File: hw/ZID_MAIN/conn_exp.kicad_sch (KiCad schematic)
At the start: 64 parts, among them J10 USB-C PWR ONLY, J8 BRK EXP SOCKET, J9 Z80-TARGET, U24 74AHCT125

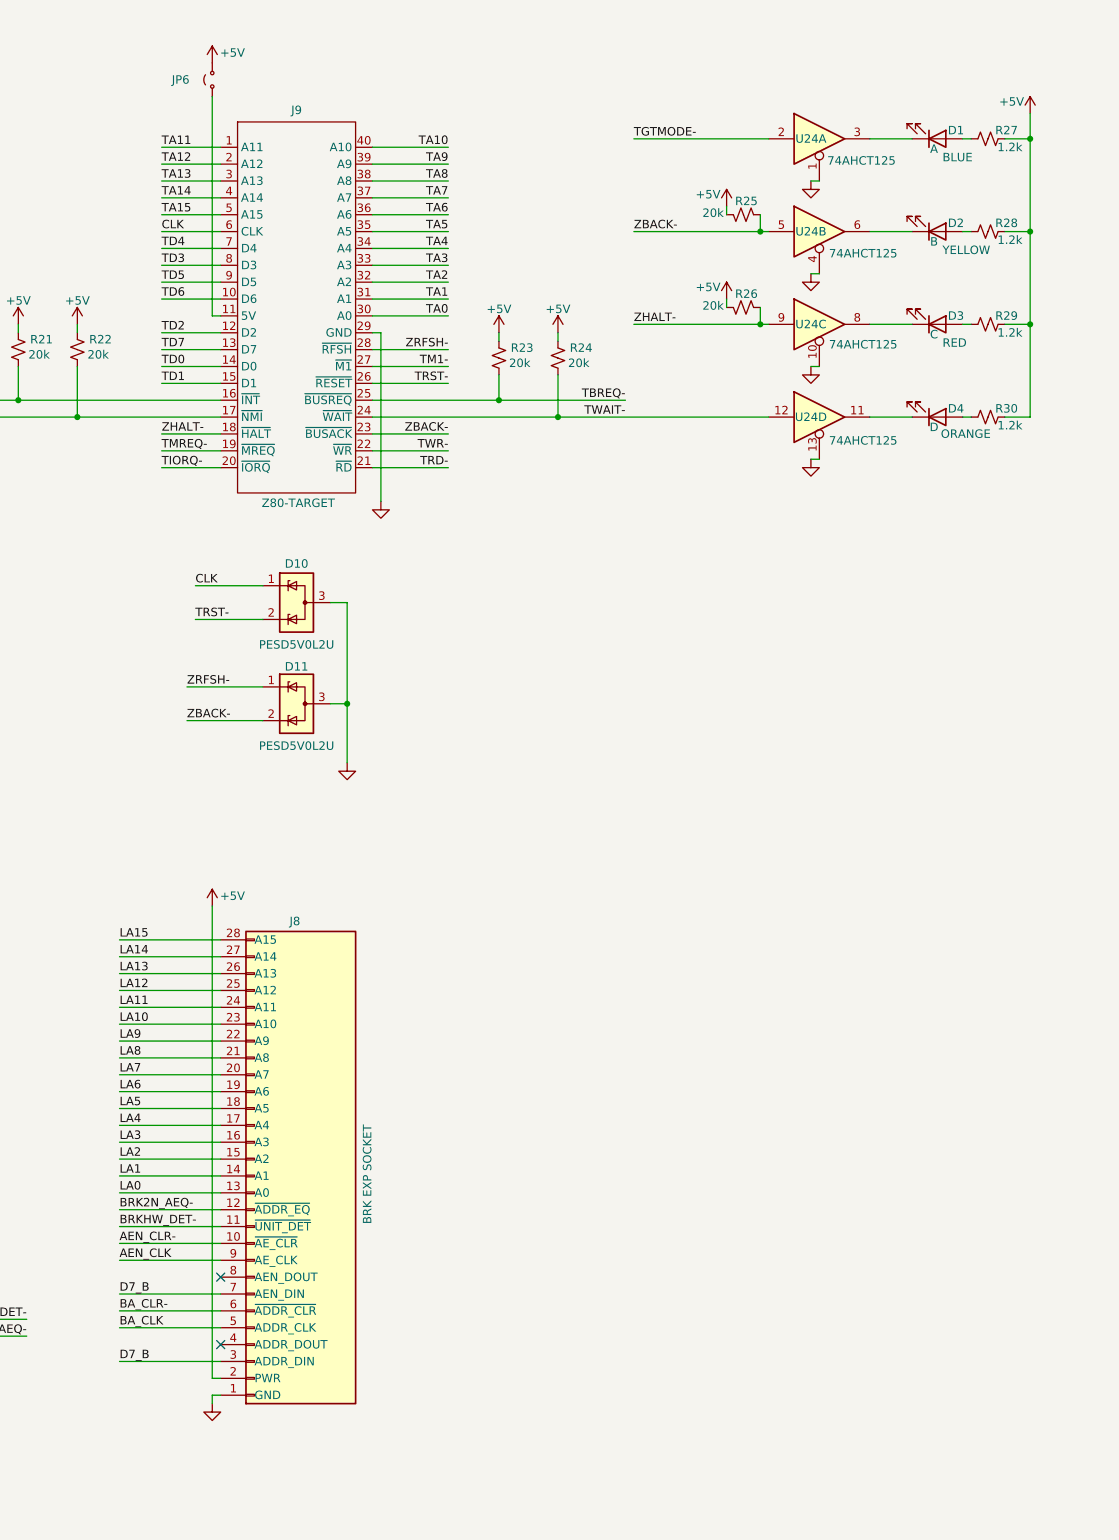
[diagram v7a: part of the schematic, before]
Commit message: Break exp conn 2x20
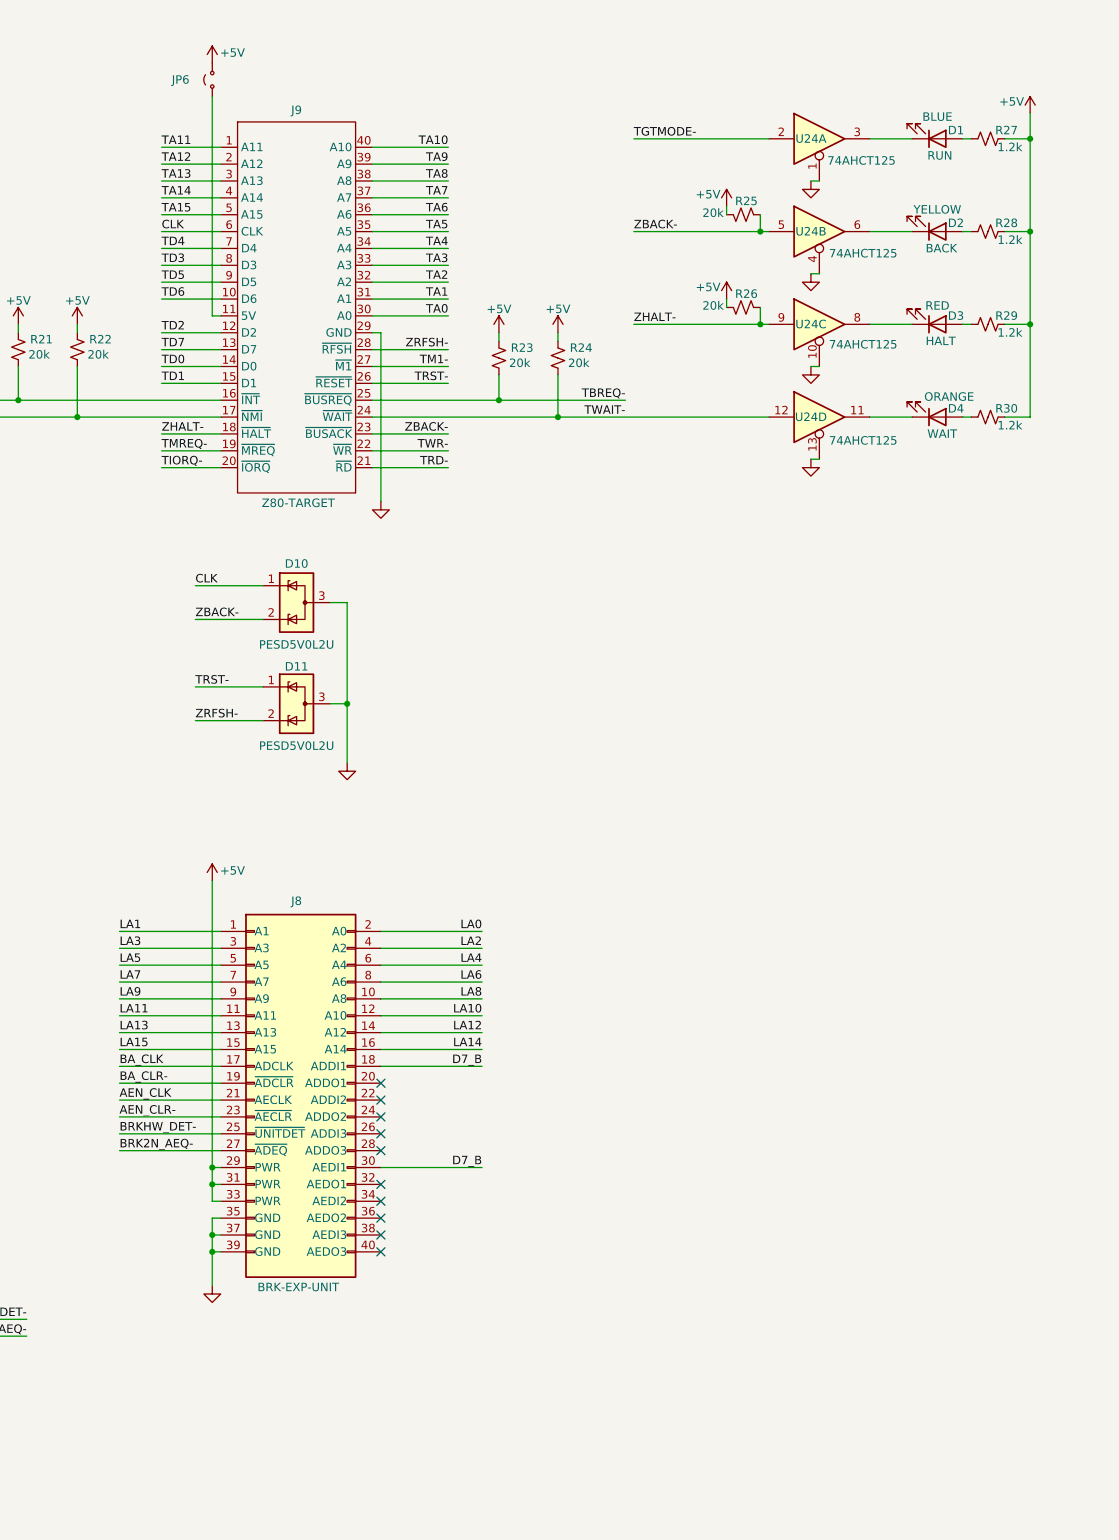
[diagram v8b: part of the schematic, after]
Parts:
- D1: Function BLUE -> RUN; Ind A -> BLUE
- D2: Function YELLOW -> BACK; Ind B -> YELLOW
- D3: Function RED -> HALT; Ind C -> RED
- D4: Function ORANGE -> WAIT; Ind D -> ORANGE
- J8: value BRK EXP SOCKET -> BRK-EXP-UNIT; footprint Connector_PinSocket_2.54mm:PinSocket_1x28_P2.54mm_Vertical -> Connector_PinHeader_2.54mm:PinHeader_2x20_P2.54mm_Vertical
- JP5: Func2 (none) -> To TGT; Function (none) -> MODINT
- JP6: Function (none) -> TGT5V
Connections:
- net +5V: now also J8.29 (PWR), J8.31 (PWR), J8.33 (PWR); no longer J8.2 (PWR)
- net AEN_CLK: now also J8.21 (AECLK); no longer J8.9 (AE_CLK)
- net AEN_CLR-: now also J8.23 (~{AECLR}); no longer J8.10 (~{AE_CLR})
- net BA_CLK: now also J8.17 (ADCLK); no longer J8.5 (ADDR_CLK)
- net BA_CLR-: now also J8.19 (~{ADCLR}); no longer J8.6 (~{ADDR_CLR})
- net BRK2N_AEQ-: now also J8.27 (~{ADEQ}); no longer J8.12 (~{ADDR_EQ})
- net BRKHW_DET-: now also J8.25 (~{UNITDET}); no longer J8.11 (~{UNIT_DET})
- net D7_B: now also J8.18 (ADDI1), J8.30 (AEDI1); no longer J8.3 (ADDR_DIN), J8.7 (AEN_DIN)
- net GND: now also J8.35 (GND), J8.37 (GND), J8.39 (GND); no longer J8.1 (GND)
- net LA0: now also J8.2 (A0); no longer J8.13 (A0)
- net LA1: now also J8.1 (A1); no longer J8.14 (A1)
- net LA10: now also J8.12 (A10); no longer J8.23 (A10)
- net LA11: now also J8.11 (A11); no longer J8.24 (A11)
- net LA12: now also J8.14 (A12); no longer J8.25 (A12)
- net LA13: now also J8.13 (A13); no longer J8.26 (A13)
- net LA14: now also J8.16 (A14); no longer J8.27 (A14)
- net LA15: now also J8.15 (A15); no longer J8.28 (A15)
- net LA2: now also J8.4 (A2); no longer J8.15 (A2)
- net LA3: now also J8.3 (A3); no longer J8.16 (A3)
- net LA4: now also J8.6 (A4); no longer J8.17 (A4)
- net LA5: now also J8.5 (A5); no longer J8.18 (A5)
- net LA6: now also J8.8 (A6); no longer J8.19 (A6)
- net LA7: now also J8.7 (A7); no longer J8.20 (A7)
- net LA8: now also J8.10 (A8); no longer J8.21 (A8)
- net LA9: now also J8.9 (A9); no longer J8.22 (A9)
- net TRST-: now also D11.1 (K); no longer D10.2 (K)
- net ZBACK-: now also D10.2 (K); no longer D11.2 (K)
- net ZRFSH-: now also D11.2 (K); no longer D11.1 (K)
- no-connect marks 10 -> 18
